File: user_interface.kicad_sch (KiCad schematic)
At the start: 26 parts, among them J1201 PH1-07-UA, J1202 EMI shield frame, J1203 FH12A-40S-0.5SH(55), U1201 TCA9554PW, U1202 AP5725FDCG-7, X1201 Keypad 3x4, X1202 NHD-4.3-480272EF-ASXP

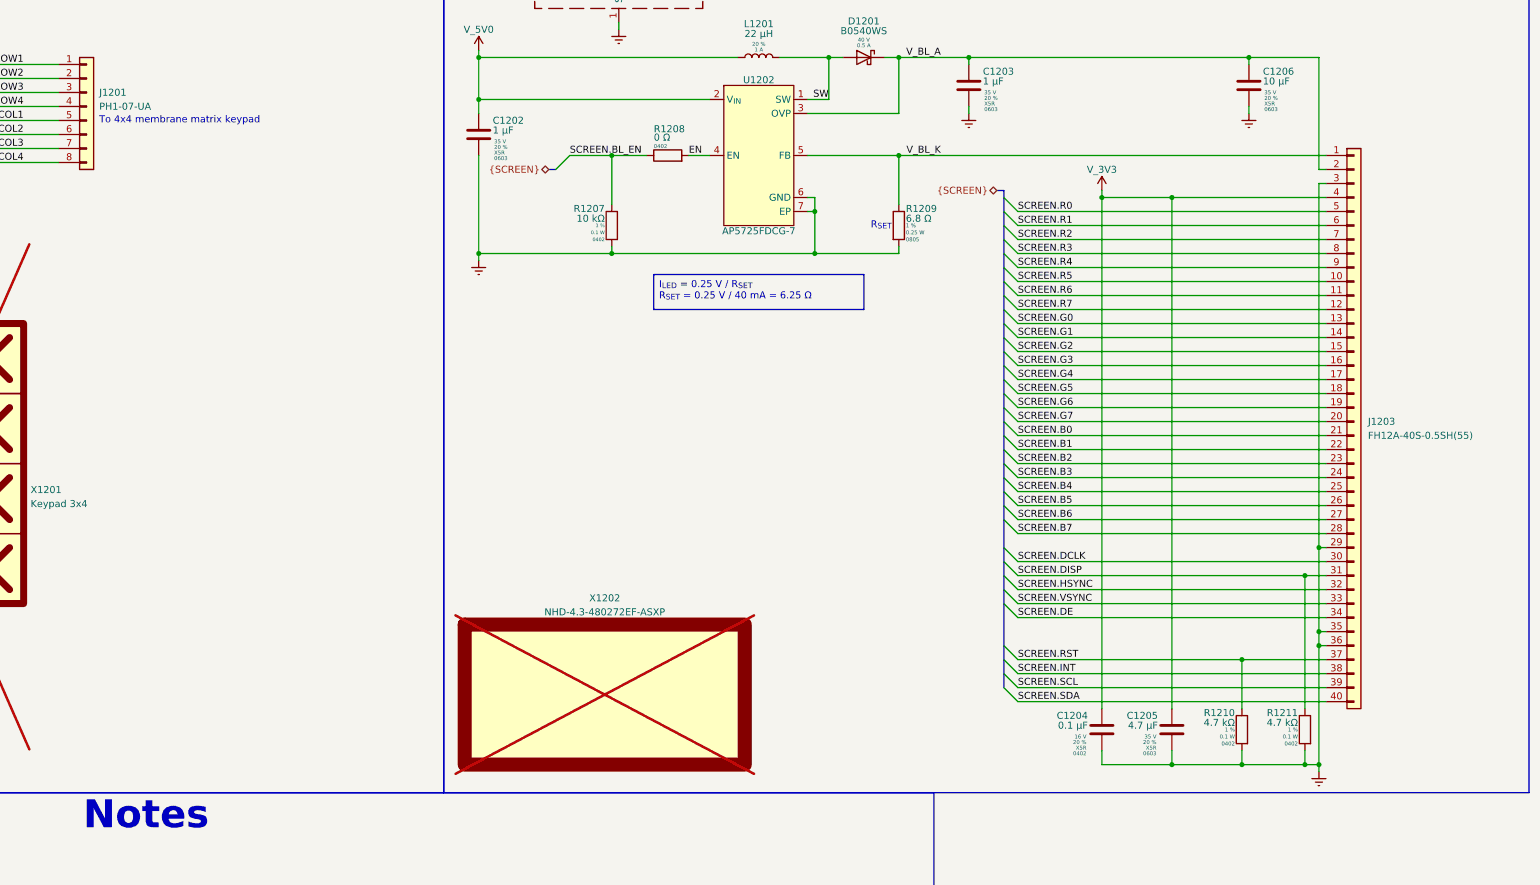
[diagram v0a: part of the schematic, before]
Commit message: Fix BOM and symbols
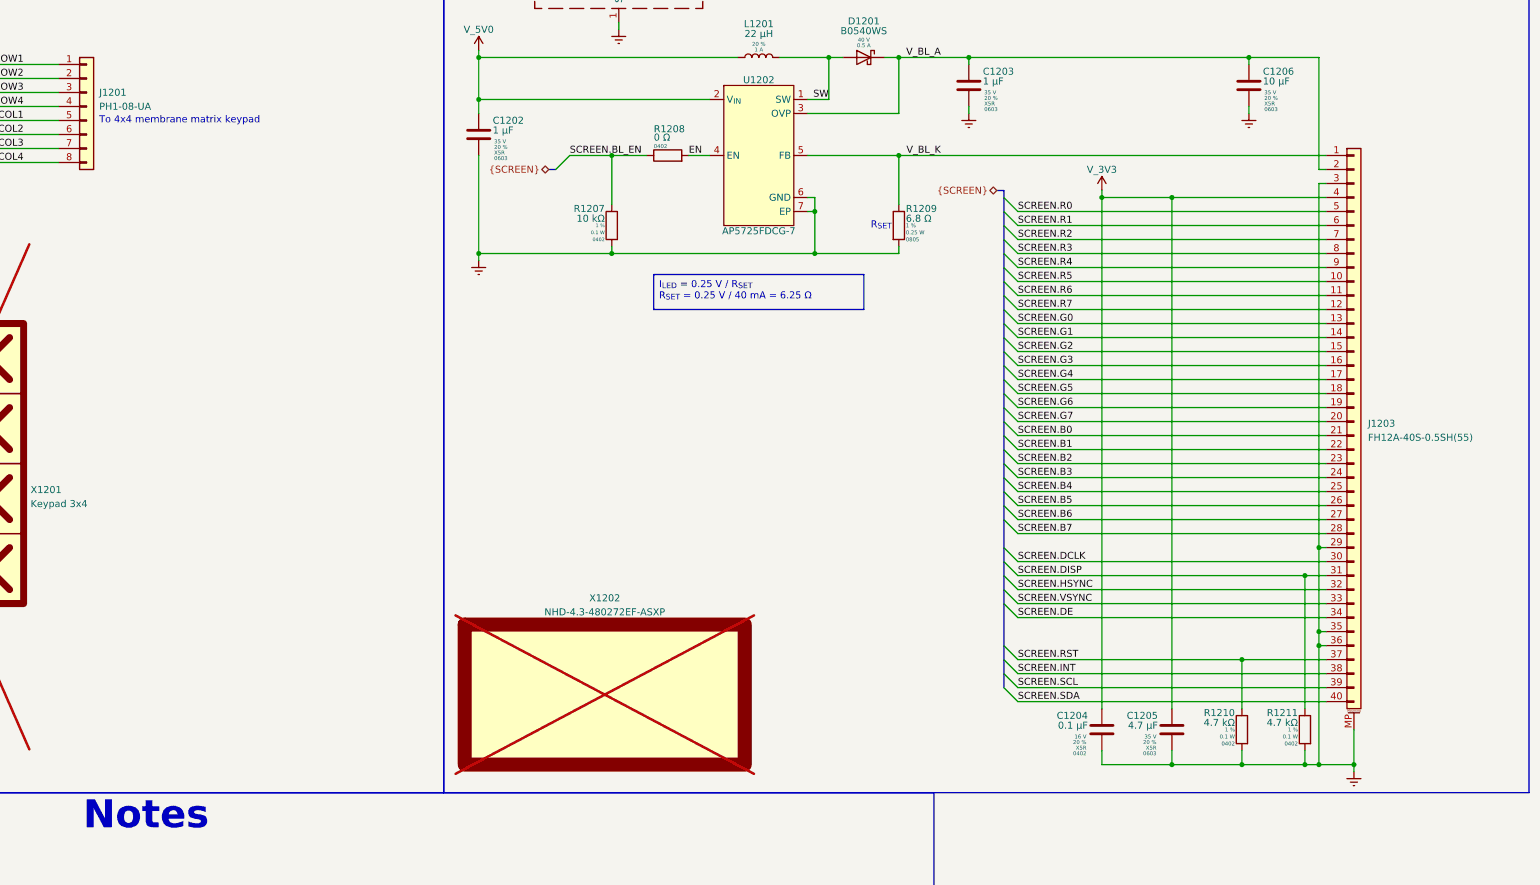
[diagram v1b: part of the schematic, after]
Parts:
- J1201: value PH1-07-UA -> PH1-08-UA; footprint Connector_PinHeader_2.54mm:PinHeader_1x07_P2.54mm_Vertical -> Connector_PinHeader_2.54mm:PinHeader_1x08_P2.54mm_Vertical; Digi-Key Part Number 2057-PH1-07-UA-ND -> 2057-PH1-08-UA-ND; MPN PH1-07-UA -> PH1-08-UA
- J1203: symbol Connector_Generic:Conn_01x40 -> Connector_Generic_MountingPin:Conn_01x40_MountingPin
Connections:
- net GND: now also J1203.MP (MountPin)
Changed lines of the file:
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@@
 	)
 	(junction
+		(at 374.65 246.38)
+		(diameter 0)
+		(color 0 0 0 0)
+	)
+	(junction
 		(at 240.03 153.67)
 		(diameter 0)
@@
 	(wire
 		(pts
+			(xy 374.65 246.38) (xy 368.3 246.38)
+		)
+		(stroke
+			(width 0)
+			(type default)
+		)
+	)
+	(wire
+		(pts
 			(xy 313.69 184.15) (xy 369.57 184.15)
 		)
@@
 	(wire
 		(pts
-			(xy 368.3 247.65) (xy 368.3 246.38)
+			(xy 374.65 247.65) (xy 374.65 246.38)
 		)
 		(stroke
@@
 	(wire
 		(pts
+			(xy 374.65 240.03) (xy 374.65 246.38)
+		)
+		(stroke
+			(width 0)
+			(type default)
+		)
+	)
+	(wire
+		(pts
 			(xy 313.69 146.05) (xy 369.57 146.05)
 		)
@@
 	(symbol
 		(lib_id "power:Earth")
-		(at 368.3 247.65 0)
+		(at 374.65 247.65 0)
 		(unit 1)
 		(exclude_from_sim no)
@@
 		(fields_autoplaced yes)
 		(property "Reference" "#PWR01209"
-			(at 368.3 254 0)
+			(at 374.65 254 0)
 			(effects
 				(font
@@
 		)
 		(property "Value" "GND"
-			(at 368.3 252.73 0)
+			(at 374.65 252.73 0)
 			(effects
 				(font
@@
 		)
 		(property "Footprint" ""
-			(at 368.3 247.65 0)
+			(at 374.65 247.65 0)
 			(effects
 				(font
@@
 		)
 		(property "Datasheet" "~"
-			(at 368.3 247.65 0)
+			(at 374.65 247.65 0)
 			(effects
 				(font
@@
 		)
 		(property "Description" "Power symbol creates a global label with name \"Earth\""
-			(at 368.3 247.65 0)
+			(at 374.65 247.65 0)
 			(effects
 				(font
@@
 			)
 		)
-		(property "Value" "PH1-07-UA"
+		(property "Value" "PH1-08-UA"
 			(at 147.066 127 0)
 			(effects
@@
 			)
 		)
-		(property "Footprint" "Connector_PinHeader_2.54mm:PinHeader_1x07_P2.54mm_Vertical"
+		(property "Footprint" "Connector_PinHeader_2.54mm:PinHeader_1x08_P2.54mm_Vertical"
 			(at 144.78 127 0)
 			(effects
@@
 			)
 		)
-		(property "Description" "Connector Header Through Hole 7 position 0.100\" (2.54mm)"
+		(property "Description" "Connector Header Through Hole 8 position 0.100\" (2.54mm)"
 			(at 144.78 127 0)
 			(effects
@@
 			)
 		)
-		(property "Digi-Key Part Number" "2057-PH1-07-UA-ND"
+		(property "Digi-Key Part Number" "2057-PH1-08-UA-ND"
 			(at 144.78 127 0)
 			(effects
@@
 			)
 		)
-		(property "MPN" "PH1-07-UA"
+		(property "MPN" "PH1-08-UA"
 			(at 144.78 127 0)
 			(effects
@@
 	)
 	(symbol
-		(lib_id "Connector_Generic:Conn_01x40")
+		(lib_id "Connector_Generic_MountingPin:Conn_01x40_MountingPin")
 		(at 374.65 184.15 0)
 		(unit 1)
@@
 		(fields_autoplaced yes)
 		(property "Reference" "J1203"
-			(at 377.19 184.1499 0)
+			(at 377.19 184.5055 0)
 			(effects
 				(font
@@
 		)
 		(property "Value" "FH12A-40S-0.5SH(55)"
-			(at 377.19 186.6899 0)
+			(at 377.19 187.0455 0)
 			(effects
 				(font
@@
 			)
 		)
-		(property "Datasheet" "https://www.hirose.com/product/document?clcode=&productname=&series=FH12&documenttype=Catalog&lang=en&documentid=D31648_en"
+		(property "Datasheet" "~"
 			(at 374.65 184.15 0)
 			(effects
@@
 			)
 		)
-		(property "Description" "40 Position FFC, FPC Connector Contacts, Top 0.020\" (0.50mm) Surface Mount, Right Angle"
+		(property "Description" "Generic connectable mounting pin connector, single row, 01x40, script generated (kicad-library-utils/schlib/autogen/connector/)"
 			(at 374.65 184.15 0)
 			(effects
@@
 		(pin "39"
 		)
+		(pin "MP"
+		)
 		(instances

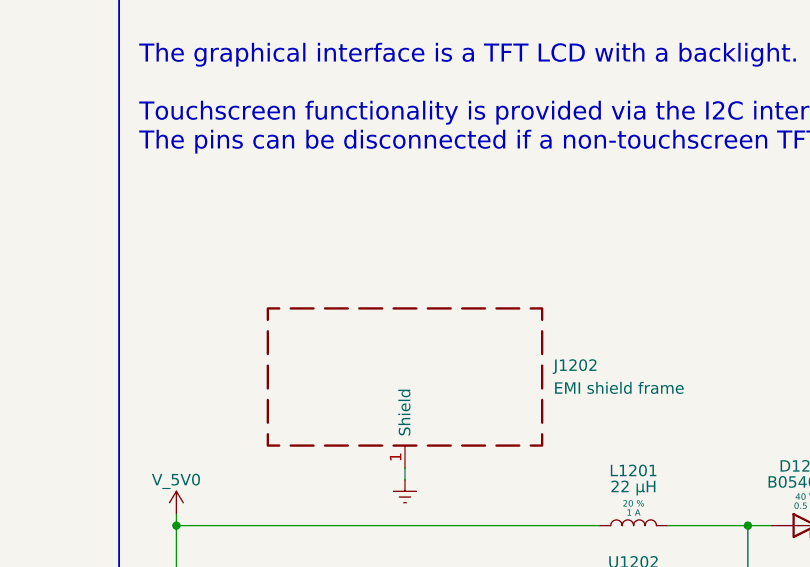
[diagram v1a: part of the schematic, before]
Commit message: Connect ESD TVS to chassis where possible, update version and date
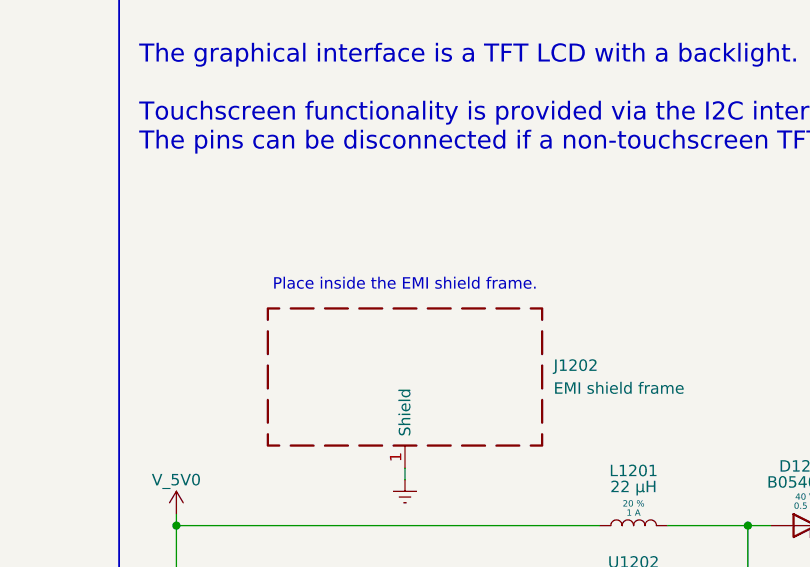
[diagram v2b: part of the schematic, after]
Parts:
- J1202: footprint RF_Shielding:Laird_Technologies_BMI-S-202-F_16.50x16.50mm -> RF_Shielding:Laird_Technologies_BMI-S-203-F_26.21x26.21mm
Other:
- note added: "Place inside the EMI shield frame."
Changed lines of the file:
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@@
 	(title_block
 		(title "Linux SBC")
-		(date "2025-11-07")
-		(rev "v0.0.1")
+		(date "2025-12-14")
+		(rev "v1.0.0")
 	)
 	(bus_alias "SCREEN"
@@
 		)
 	)
+	(text "Place inside the EMI shield frame."
+		(exclude_from_sim no)
+		(at 241.3 91.44 0)
+		(effects
+			(font
+				(size 1.27 1.27)
+			)
+		)
+	)
 	(text_box "I_{LED} = 0.25 V / R_{SET}\nR_{SET} = 0.25 V / 40 mA = 6.25 Ω"
 		(exclude_from_sim no)
@@
 			)
 		)
-		(property "Footprint" "RF_Shielding:Laird_Technologies_BMI-S-202-F_16.50x16.50mm"
+		(property "Footprint" "RF_Shielding:Laird_Technologies_BMI-S-203-F_26.21x26.21mm"
 			(at 241.3 104.14 0)
 			(effects

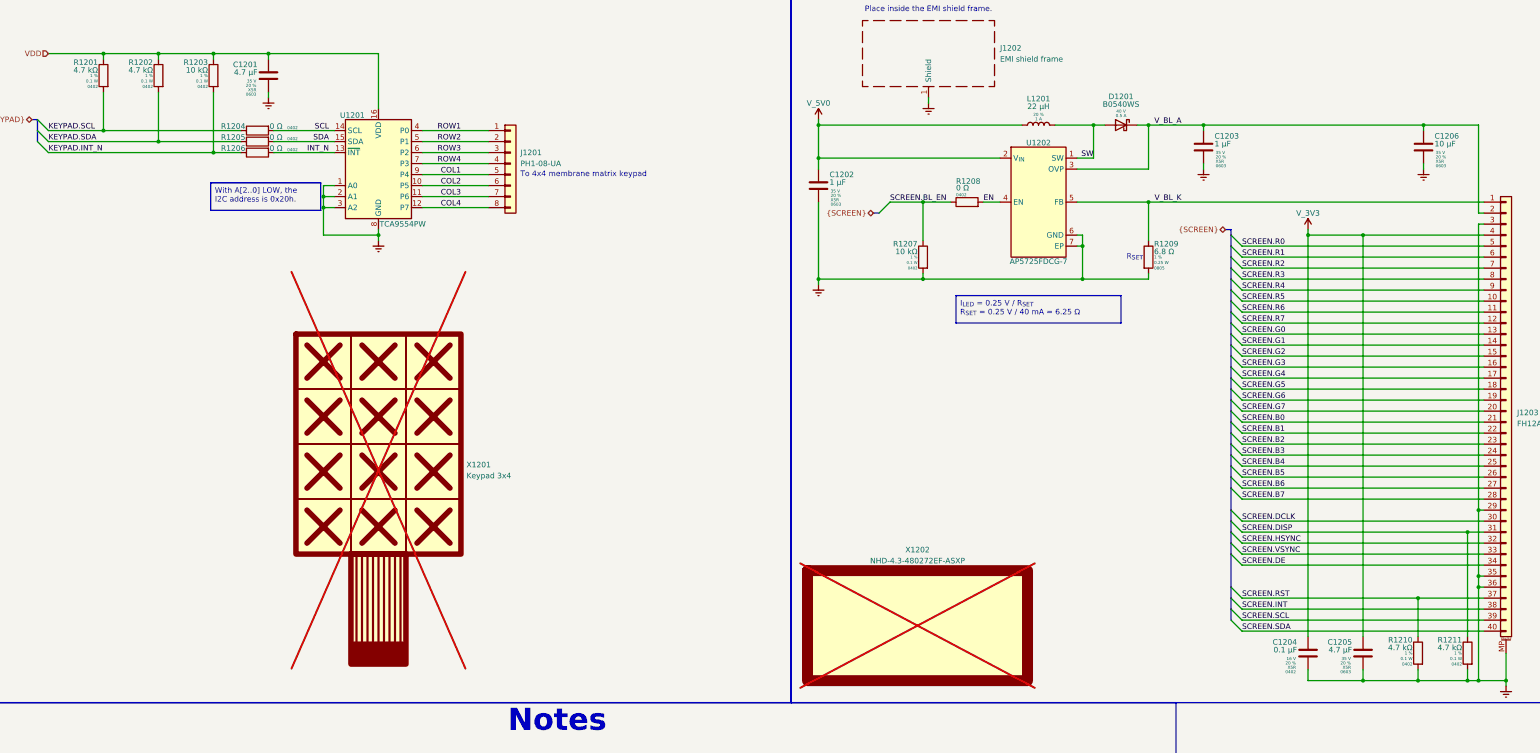
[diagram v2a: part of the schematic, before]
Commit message: 0402 -> 0201 where possible
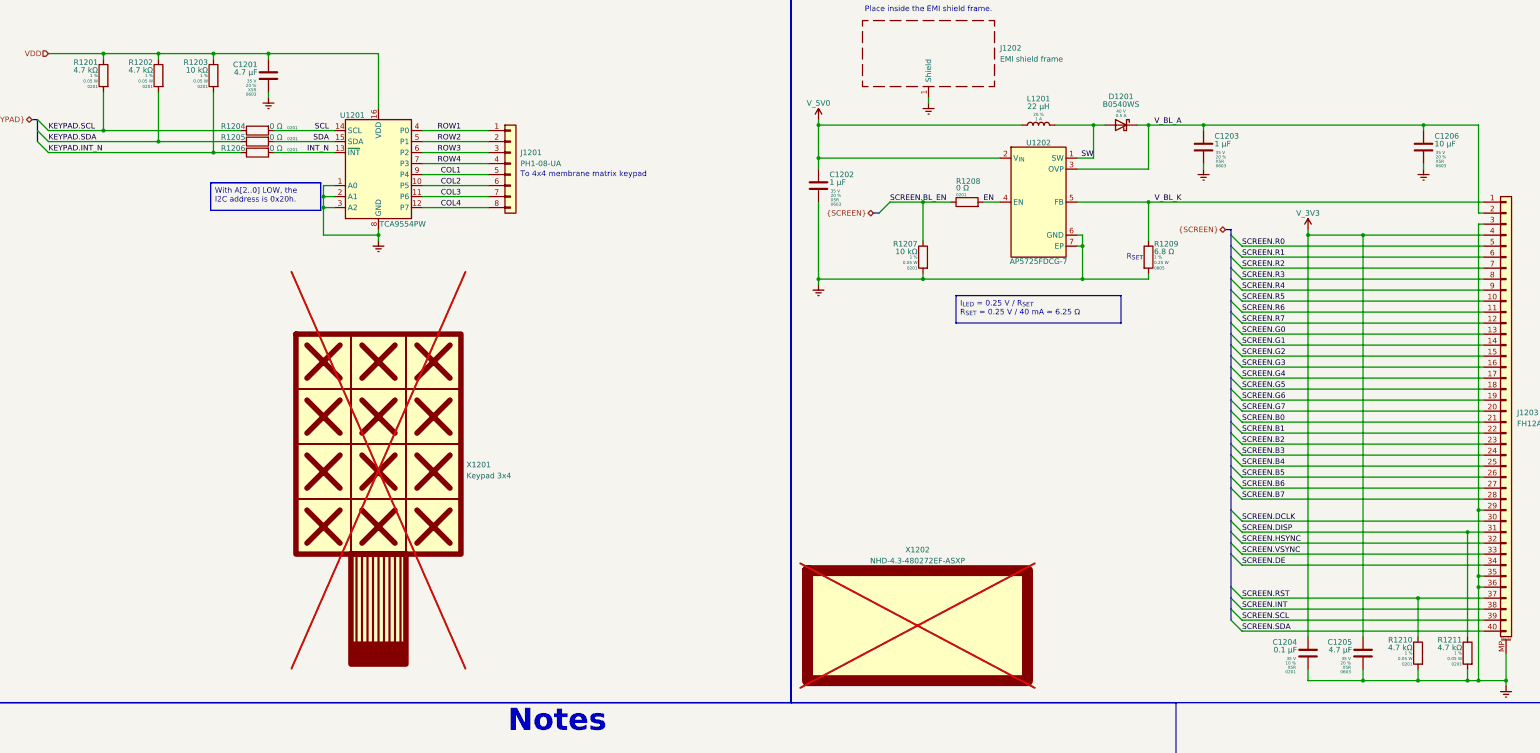
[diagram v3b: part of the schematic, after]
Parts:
- C1204: footprint perfect_footprints:C_0402_1005Metric -> Capacitor_SMD:C_0201_0603Metric; Digi-Key Part Number 490-10700-1-ND -> 490-10430-1-ND; MPN GRM155R71H104KE14D -> GRM033R6YA104KE14D; Size 0402 -> 0201; Tolerance 20 % -> 10 %; Voltage rating 16 V -> 35 V
- R1201, R1202, R1210, R1211: footprint perfect_footprints:R_0402_1005Metric -> Resistor_SMD:R_0201_0603Metric; Digi-Key Part Number P4.70KLCT-ND -> P123031CT-ND; MPN ERJ-2RKF4701X -> ERJ-1GNF4701C; Power rating 0.1 W -> 0.05 W; Size 0402 -> 0201
- R1203, R1207: footprint perfect_footprints:R_0402_1005Metric -> Resistor_SMD:R_0201_0603Metric; Digi-Key Part Number P10.0KLCT-ND -> P122414CT-ND; MPN ERJ-2RKF1002X -> ERJ-1GNF1002C; Power rating 0.1 W -> 0.05 W; Size 0402 -> 0201
- R1204, R1205, R1206, R1208: footprint perfect_footprints:R_0402_1005Metric -> Resistor_SMD:R_0201_0603Metric; Digi-Key Part Number P0.0JCT-ND -> P15979CT-ND; MPN ERJ-2GE0R00X -> ERJ-1GN0R00C; Size 0402 -> 0201

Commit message: Update BOM, and fix MPU pinout
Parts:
- C1204: footprint Capacitor_SMD:C_0201_0603Metric -> perfect_footprints:C_0201_0603Metric
- R1201, R1202, R1203, R1204, R1205, R1206, R1207, R1208, R1210, R1211: footprint Resistor_SMD:R_0201_0603Metric -> perfect_footprints:R_0201_0603Metric
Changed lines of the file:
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@@
 			)
 		)
-		(property "Footprint" "Resistor_SMD:R_0201_0603Metric"
+		(property "Footprint" "perfect_footprints:R_0201_0603Metric"
 			(at 367.538 240.03 90)
 			(effects
@@
 			)
 		)
-		(property "Footprint" "Resistor_SMD:R_0201_0603Metric"
+		(property "Footprint" "perfect_footprints:R_0201_0603Metric"
 			(at 250.19 137.668 90)
 			(effects
@@
 			)
 		)
-		(property "Footprint" "Resistor_SMD:R_0201_0603Metric"
+		(property "Footprint" "perfect_footprints:R_0201_0603Metric"
 			(at 86.36 117.602 90)
 			(effects
@@
 			)
 		)
-		(property "Footprint" "Resistor_SMD:R_0201_0603Metric"
+		(property "Footprint" "perfect_footprints:R_0201_0603Metric"
 			(at 86.36 122.682 90)
 			(effects
@@
 			)
 		)
-		(property "Footprint" "Resistor_SMD:R_0201_0603Metric"
+		(property "Footprint" "perfect_footprints:R_0201_0603Metric"
 			(at 77.978 106.68 90)
 			(effects
@@
 			)
 		)
-		(property "Footprint" "Resistor_SMD:R_0201_0603Metric"
+		(property "Footprint" "perfect_footprints:R_0201_0603Metric"
 			(at 241.808 148.59 90)
 			(effects
@@
 			)
 		)
-		(property "Footprint" "Resistor_SMD:R_0201_0603Metric"
+		(property "Footprint" "perfect_footprints:R_0201_0603Metric"
 			(at 52.578 106.68 90)
 			(effects
@@
 			)
 		)
-		(property "Footprint" "Resistor_SMD:R_0201_0603Metric"
+		(property "Footprint" "perfect_footprints:R_0201_0603Metric"
 			(at 356.108 240.03 90)
 			(effects
@@
 			)
 		)
-		(property "Footprint" "Resistor_SMD:R_0201_0603Metric"
+		(property "Footprint" "perfect_footprints:R_0201_0603Metric"
 			(at 86.36 120.142 90)
 			(effects
@@
 			)
 		)
-		(property "Footprint" "Capacitor_SMD:C_0201_0603Metric"
+		(property "Footprint" "perfect_footprints:C_0201_0603Metric"
 			(at 327.9648 243.84 0)
 			(effects
@@
 			)
 		)
-		(property "Footprint" "Resistor_SMD:R_0201_0603Metric"
+		(property "Footprint" "perfect_footprints:R_0201_0603Metric"
 			(at 65.278 106.68 90)
 			(effects

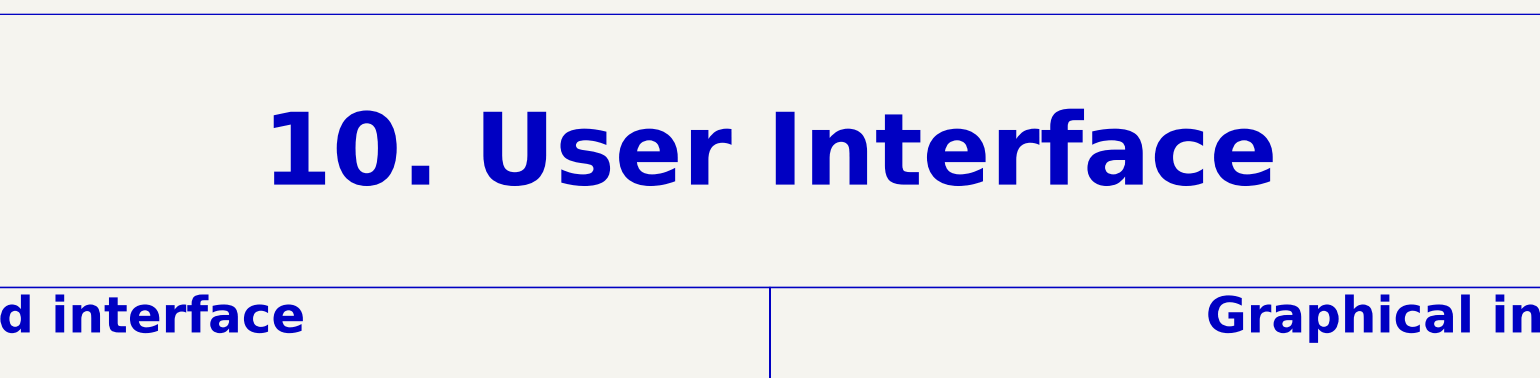
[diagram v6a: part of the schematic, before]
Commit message: Rework the schematics
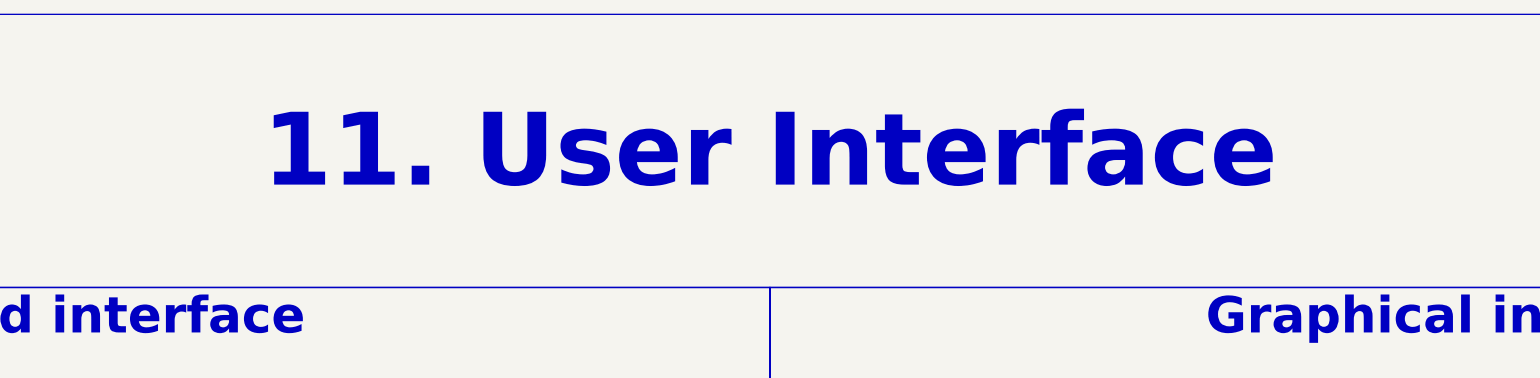
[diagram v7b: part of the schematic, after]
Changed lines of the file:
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@@
 	(title_block
 		(title "Linux SBC")
-		(date "2025-12-17")
+		(date "2025-12-19")
 		(rev "v1.0.0")
 	)
@@
 		)
 	)
-	(text_box "10. User Interface"
+	(text_box "11. User Interface"
 		(exclude_from_sim no)
 		(at 12.7 12.7 0)
